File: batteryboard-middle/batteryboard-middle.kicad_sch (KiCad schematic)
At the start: 7 parts, among them J1 Conn 02x10 1.27mm, J2 Conn_01x02, J3 Conn_01x02

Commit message: modified connector arrangement
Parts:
- removed J1: Conn 02x10 1.27mm, Connector_PinHeader_1.27mm:PinHeader_2x10_P1.27mm_Vertical, symbol Connector_Generic:Conn_02x10_Odd_Even
- added J?: Conn_01x12, symbol Connector_Generic:Conn_01x12
- added J?: Conn_01x10, symbol Connector_Generic:Conn_01x10
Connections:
- new net: J?.10 (Pin_10), J?.8 (Pin_8)
- new net: J?.11 (Pin_11), J?.9 (Pin_9)
- new net: J?.10 (Pin_10), J?.12 (Pin_12)
- new net: J?.1 (Pin_1), J?.3 (Pin_3)
- new net: J?.2 (Pin_2), J?.4 (Pin_4)
- new net: J?.3 (Pin_3), J?.5 (Pin_5)
- new net: J?.4 (Pin_4), J?.6 (Pin_6)
- new net: J?.5 (Pin_5), J?.7 (Pin_7)
- new net: J?.6 (Pin_6), J?.8 (Pin_8)
- new net: J?.7 (Pin_7), J?.9 (Pin_9)
- no-connect marks 16 -> 0
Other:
- note added: "Stack Conn - From Batteryboard Bottom"
- note added: "Stack Conn - To Batteryboard Top"
- note removed: "Stack Conn"
- moved on the sheet: J2, J3

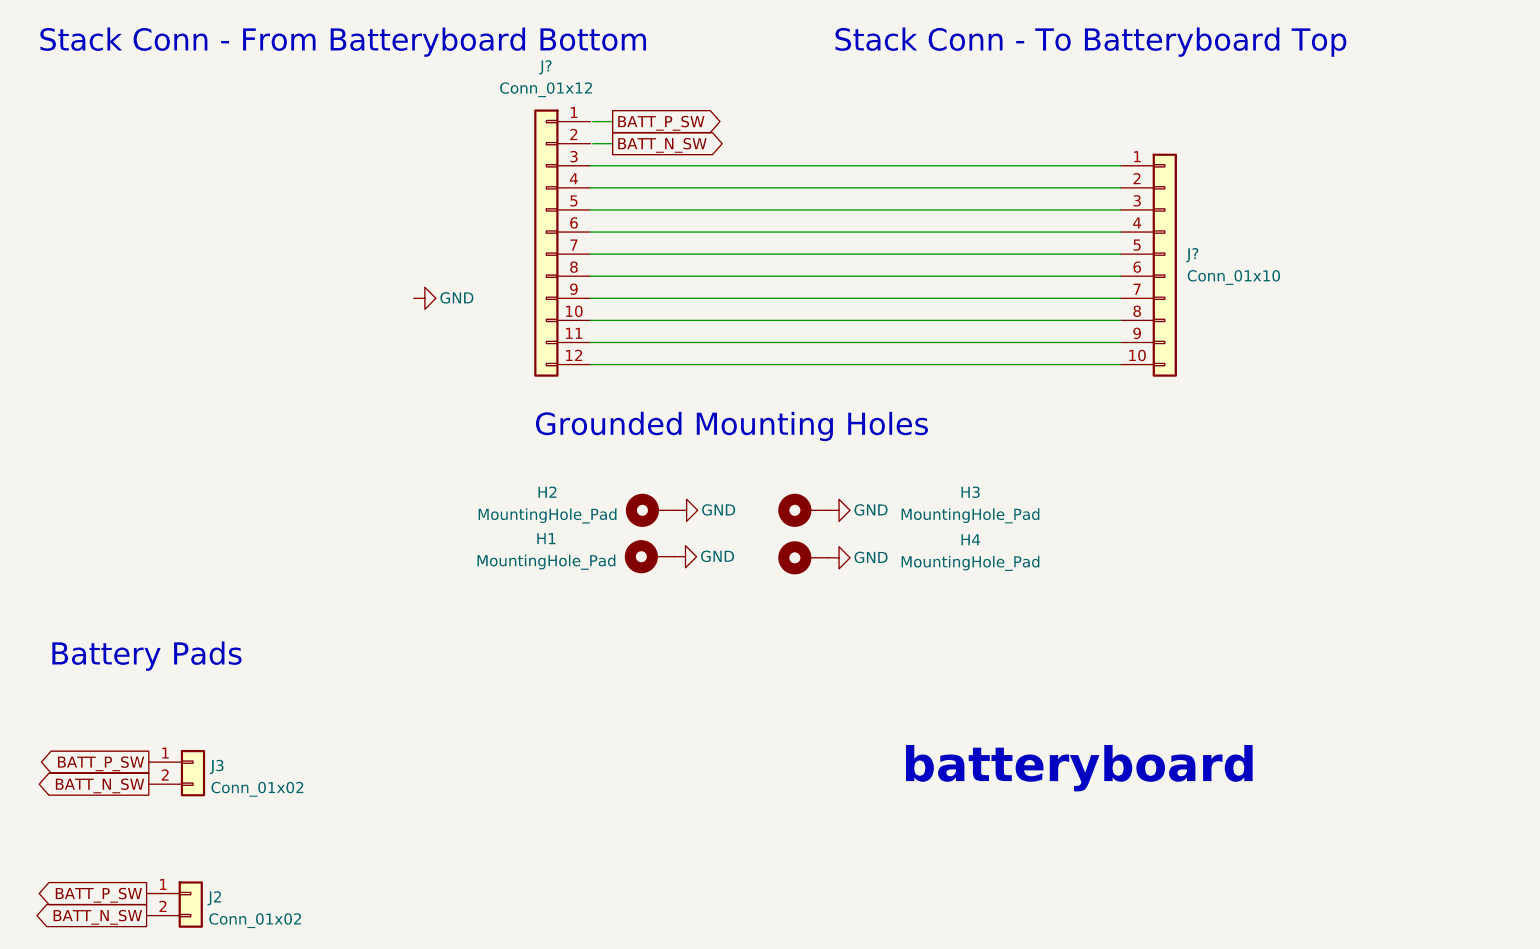
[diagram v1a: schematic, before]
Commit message: labeled connections
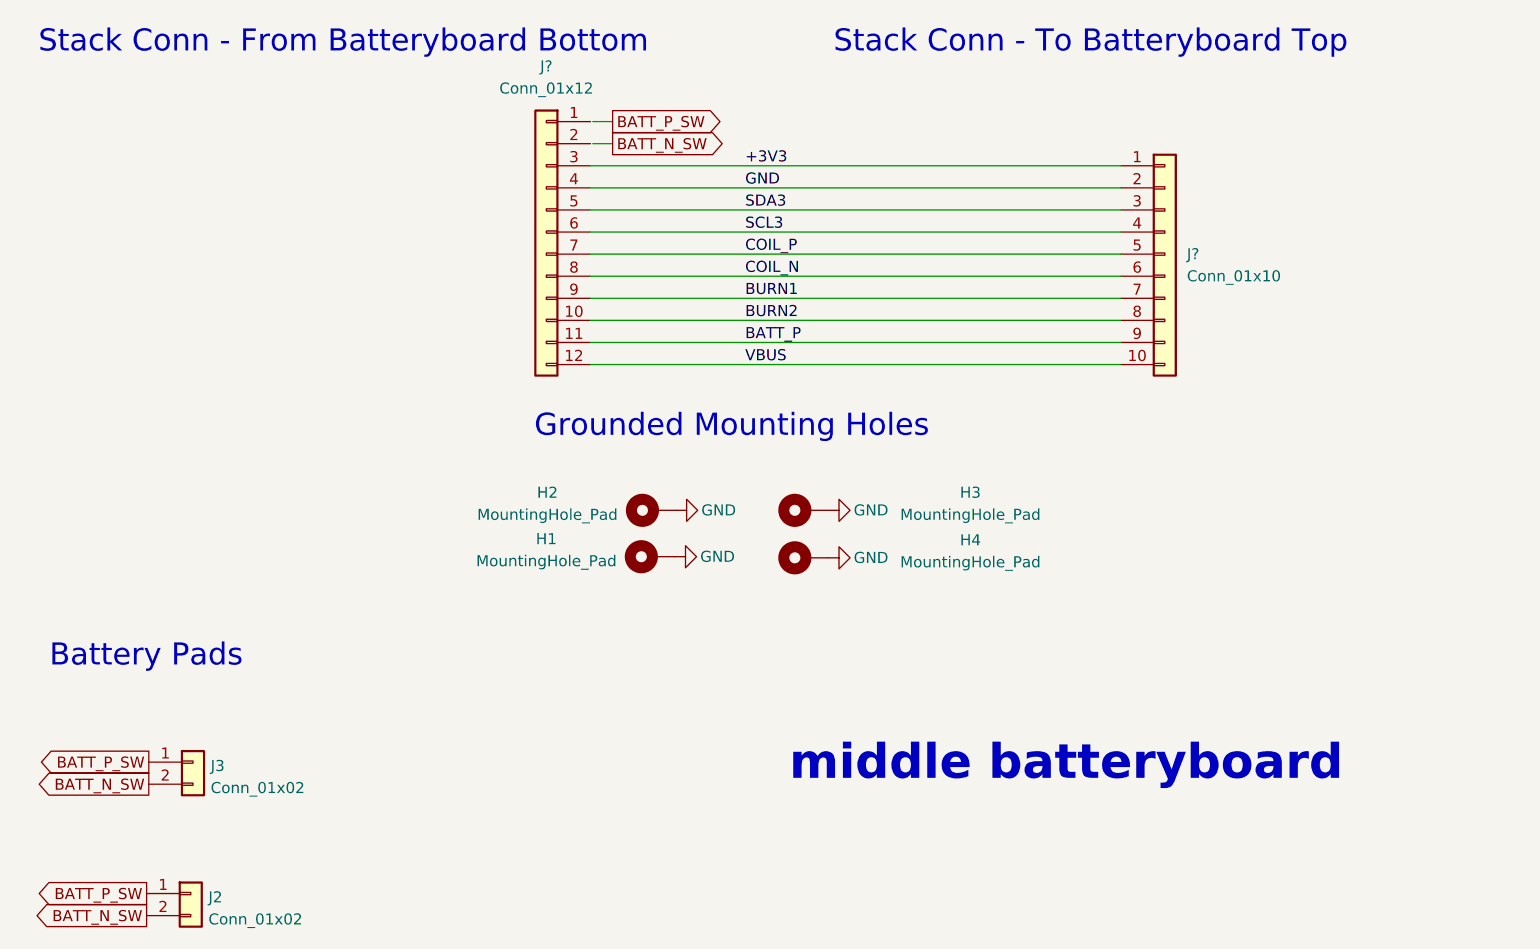
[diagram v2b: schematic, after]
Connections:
- net GND: now also J?.2 (Pin_2), J?.4 (Pin_4)
- net BURN2: now reaches J?.10 (Pin_10), J?.8 (Pin_8)
- net BATT_P: now reaches J?.11 (Pin_11), J?.9 (Pin_9)
- net VBUS: now reaches J?.10 (Pin_10), J?.12 (Pin_12)
- net +3V3: now reaches J?.1 (Pin_1), J?.3 (Pin_3)
- net SDA3: now reaches J?.3 (Pin_3), J?.5 (Pin_5)
- net SCL3: now reaches J?.4 (Pin_4), J?.6 (Pin_6)
- net COIL_P: now reaches J?.5 (Pin_5), J?.7 (Pin_7)
- net COIL_N: now reaches J?.6 (Pin_6), J?.8 (Pin_8)
- net BURN1: now reaches J?.7 (Pin_7), J?.9 (Pin_9)
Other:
- note added: "middle batteryboard"
- note removed: "batteryboard"
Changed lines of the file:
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@@
     (effects (font (size 2.54 2.54)) (justify left bottom))
   )
-  (text "batteryboard" (at 124.714 114.681 0)
+  (text "middle batteryboard" (at 111.76 114.3 0)
     (effects (font (size 3.9878 3.9878) (thickness 1.016) bold) (justify left bottom))
   )
   (text "Battery Pads" (at 26.67 101.092 0)
     (effects (font (size 2.54 2.54)) (justify left bottom))
+  )
+  (label "GND" (at 106.68 45.72 0)
+    (effects (font (size 1.27 1.27)) (justify left bottom))
+  )
+  (label "BURN1" (at 106.68 58.42 0)
+    (effects (font (size 1.27 1.27)) (justify left bottom))
+  )
+  (label "VBUS" (at 106.68 66.04 0)
+    (effects (font (size 1.27 1.27)) (justify left bottom))
+  )
+  (label "SCL3" (at 106.68 50.8 0)
+    (effects (font (size 1.27 1.27)) (justify left bottom))
+  )
+  (label "+3V3" (at 106.68 43.18 0)
+    (effects (font (size 1.27 1.27)) (justify left bottom))
+  )
+  (label "BURN2" (at 106.68 60.96 0)
+    (effects (font (size 1.27 1.27)) (justify left bottom))
+  )
+  (label "COIL_N" (at 106.68 55.88 0)
+    (effects (font (size 1.27 1.27)) (justify left bottom))
+  )
+  (label "COIL_P" (at 106.68 53.34 0)
+    (effects (font (size 1.27 1.27)) (justify left bottom))
+  )
+  (label "SDA3" (at 106.68 48.26 0)
+    (effects (font (size 1.27 1.27)) (justify left bottom))
+  )
+  (label "BATT_P" (at 106.68 63.5 0)
+    (effects (font (size 1.27 1.27)) (justify left bottom))
   )
   (global_label "BATT_P_SW" (shape output) (at 37.846 126.873 180) (fields_autoplaced)
@@
       (effects (font (size 1.27 1.27)) (justify right) hide)
     )
-  )
-  (symbol (lib_id "power:GND") (at 68.58 58.42 90) (unit 1)
-    (in_bom yes) (on_board yes)
-    (property "Reference" "#PWR?" (id 0) (at 74.93 58.42 0)
-      (effects (font (size 1.27 1.27)) hide)
-    )
-    (property "Value" "GND" (id 1) (at 73.533 58.42 90))
-    (property "Footprint" "" (id 2) (at 68.58 58.42 0)
-      (effects (font (size 1.27 1.27)) hide)
-    )
-    (property "Datasheet" "" (id 3) (at 68.58 58.42 0)
-      (effects (font (size 1.27 1.27)) hide)
-    )
-    (pin "1")
   )
   (symbol (lib_id "Connector_Generic:Conn_01x12") (at 83.82 50.8 0) (mirror y) (unit 1)
@@
       (reference "#PWR0106") (unit 1) (value "GND") (footprint "")
     )
-    (path "/1bdfede1-22a7-4a7e-8979-e030eca04f8f"
-      (reference "#PWR?") (unit 1) (value "GND") (footprint "")
-    )
     (path "/5a4e0212-db20-4e54-af24-453bc0252d21"

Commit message: switch to 2x connectors for battery boards
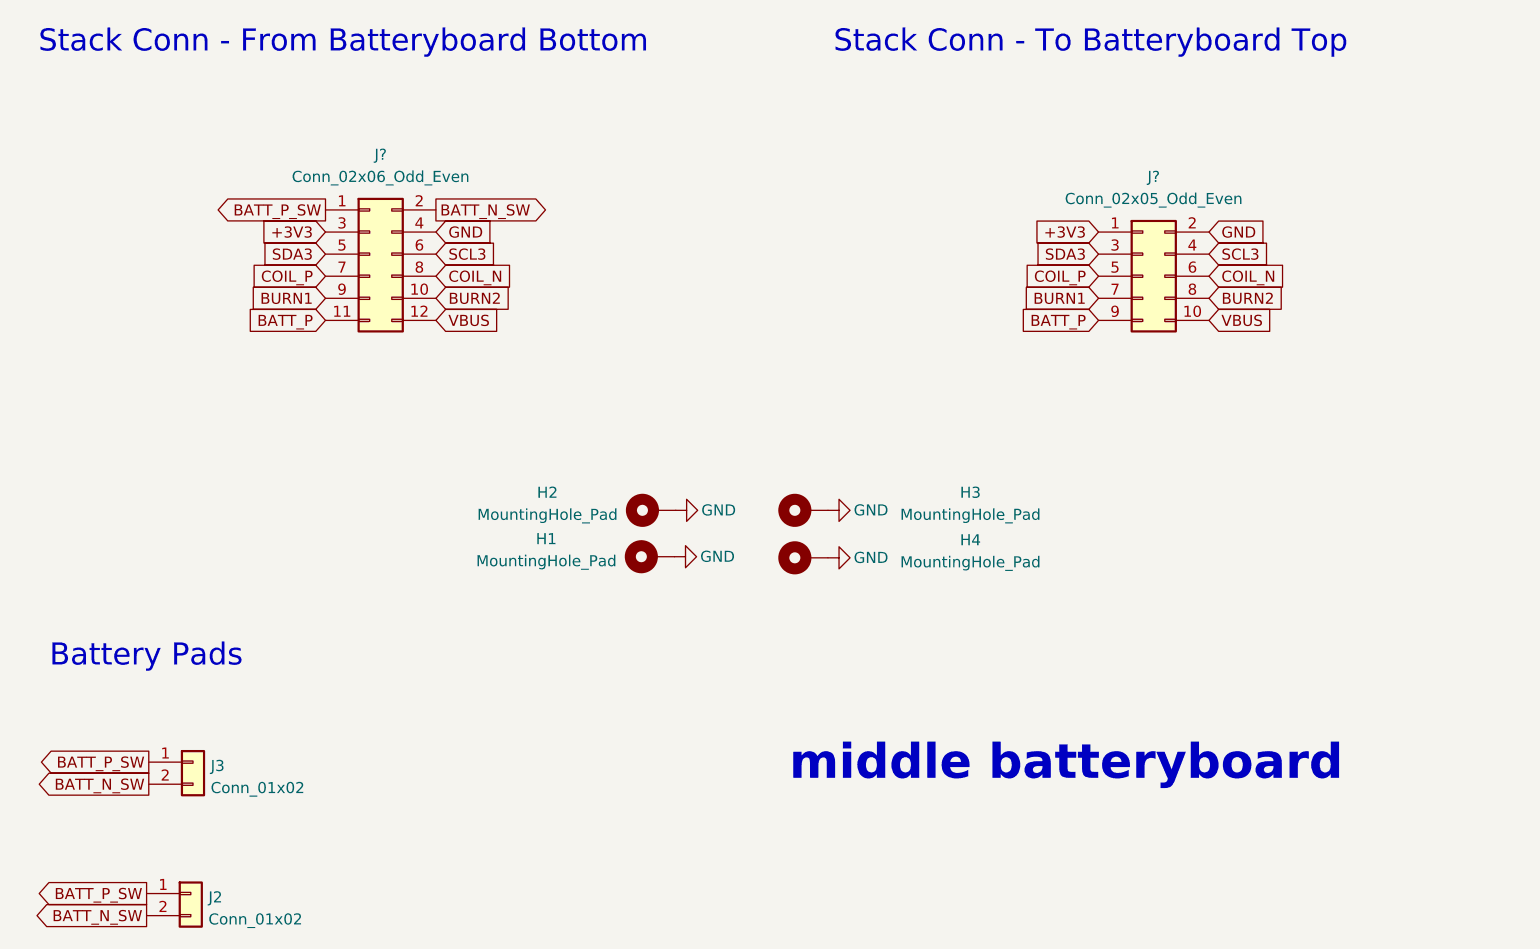
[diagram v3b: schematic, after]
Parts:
- removed J?: Conn_01x12, symbol Connector_Generic:Conn_01x12
- removed J?: Conn_01x10, symbol Connector_Generic:Conn_01x10
- added J?: Conn_02x06_Odd_Even, symbol Connector_Generic:Conn_02x06_Odd_Even
- added J?: Conn_02x05_Odd_Even, symbol Connector_Generic:Conn_02x05_Odd_Even
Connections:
- net +3V3: now also J?.1 (Pin_1), J?.3 (Pin_3)
- net BATT_N_SW: now also J?.2 (Pin_2)
- net BATT_P: now also J?.11 (Pin_11), J?.9 (Pin_9)
- net BATT_P_SW: now also J?.1 (Pin_1)
- net BURN1: now also J?.7 (Pin_7), J?.9 (Pin_9)
- net BURN2: now also J?.10 (Pin_10), J?.8 (Pin_8)
- net COIL_N: now also J?.6 (Pin_6), J?.8 (Pin_8)
- net COIL_P: now also J?.5 (Pin_5), J?.7 (Pin_7)
- net GND: now also J?.2 (Pin_2), J?.4 (Pin_4)
- net SCL3: now also J?.4 (Pin_4), J?.6 (Pin_6)
- net SDA3: now also J?.3 (Pin_3), J?.5 (Pin_5)
- net VBUS: now also J?.10 (Pin_10), J?.12 (Pin_12)
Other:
- note removed: "Grounded Mounting Holes"

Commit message: remove burn wire signals
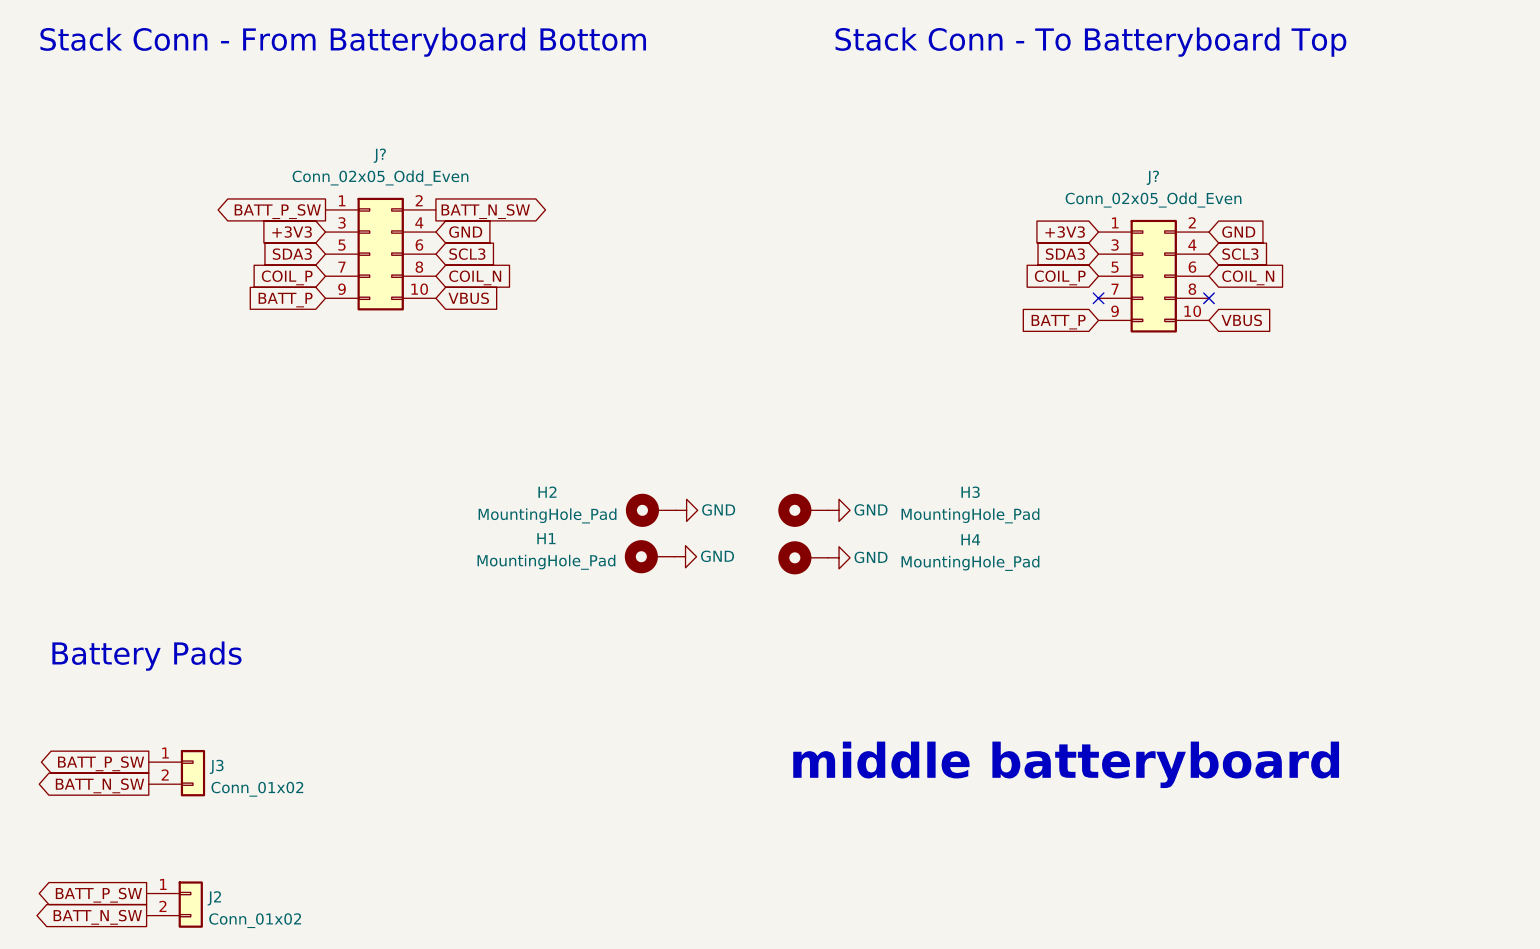
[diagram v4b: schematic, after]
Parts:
- removed J?: Conn_02x06_Odd_Even, symbol Connector_Generic:Conn_02x06_Odd_Even
- added J?: Conn_02x05_Odd_Even, symbol Connector_Generic:Conn_02x05_Odd_Even
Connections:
- net +3V3: now also J?.3 (Pin_3)
- net BATT_N_SW: now also J?.2 (Pin_2)
- net BATT_P: now also J?.9 (Pin_9)
- net BATT_P_SW: now also J?.1 (Pin_1)
- net COIL_N: now also J?.8 (Pin_8)
- net COIL_P: now also J?.7 (Pin_7)
- net GND: now also J?.4 (Pin_4)
- net SCL3: now also J?.6 (Pin_6)
- net SDA3: now also J?.5 (Pin_5)
- net VBUS: now also J?.10 (Pin_10)
- net BURN1: no longer names the net of J?.7 (Pin_7)
- net BURN2: no longer names the net of J?.8 (Pin_8)
- no-connect marks 0 -> 2

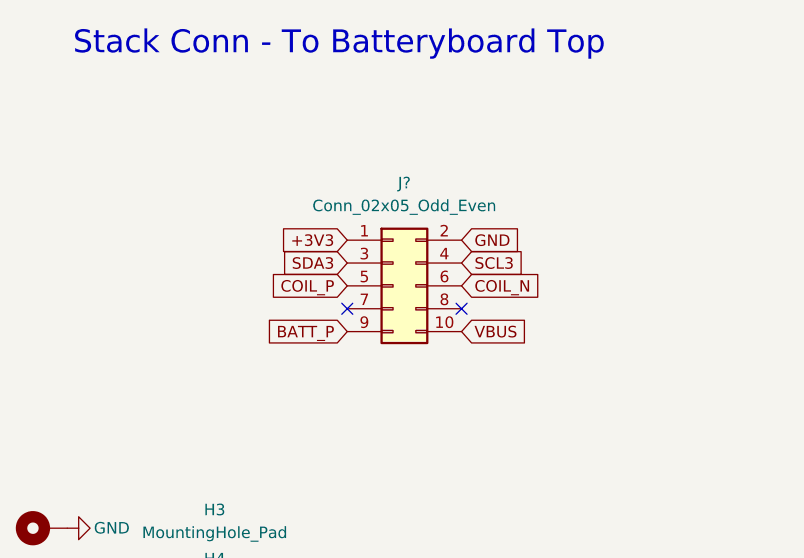
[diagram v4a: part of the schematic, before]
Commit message: NC on pins 1 and 2 to match with -Y
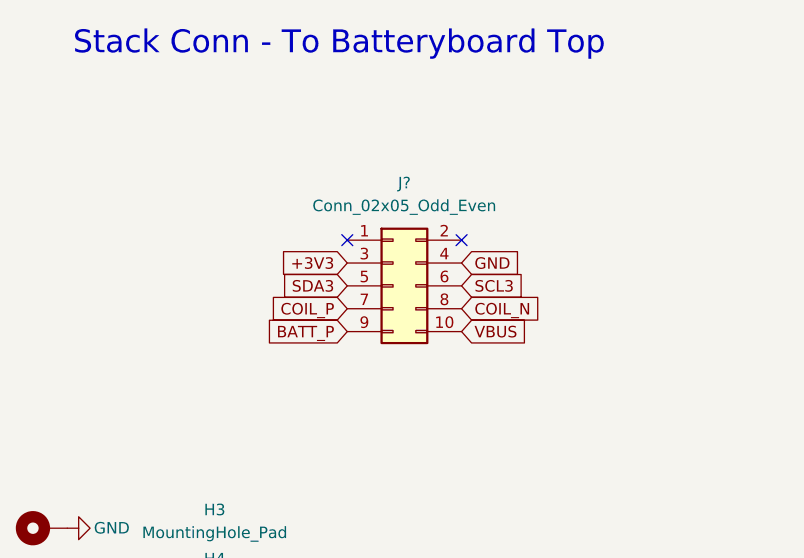
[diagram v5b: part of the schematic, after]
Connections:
- net +3V3: now also J?.3 (Pin_3); no longer J?.1 (Pin_1)
- net COIL_N: now also J?.8 (Pin_8); no longer J?.6 (Pin_6)
- net COIL_P: now also J?.7 (Pin_7); no longer J?.5 (Pin_5)
- net GND: now also J?.4 (Pin_4); no longer J?.2 (Pin_2)
- net SCL3: now also J?.6 (Pin_6); no longer J?.4 (Pin_4)
- net SDA3: now also J?.5 (Pin_5); no longer J?.3 (Pin_3)
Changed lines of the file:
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@@
     (comment 1 "N. Khera")
   )
-  (no_connect (at 147.32 58.42))
-  (no_connect (at 160.02 58.42))
+  (no_connect (at 160.02 50.8))
+  (no_connect (at 147.32 50.8))
   (text "Stack Conn - To Batteryboard Top" (at 116.84 30.48 0)
     (effects (font (size 2.54 2.54)) (justify left bottom))
@@
     )
   )
-  (global_label "SDA3" (shape input) (at 147.32 53.34 180) (fields_autoplaced)
+  (global_label "SDA3" (shape input) (at 147.32 55.88 180) (fields_autoplaced)
     (effects (font (size 1.27 1.27)) (justify right))
-    (property "Intersheet References" "${INTERSHEET_REFS}" (id 0) (at 140.1293 53.2606 0)
+    (property "Intersheet References" "${INTERSHEET_REFS}" (id 0) (at 140.1293 55.8006 0)
       (effects (font (size 1.27 1.27)) (justify right) hide)
     )
@@
     )
   )
-  (global_label "+3V3" (shape input) (at 147.32 50.8 180) (fields_autoplaced)
+  (global_label "+3V3" (shape input) (at 147.32 53.34 180) (fields_autoplaced)
     (effects (font (size 1.27 1.27)) (justify right))
-    (property "Intersheet References" "${INTERSHEET_REFS}" (id 0) (at 139.8269 50.7206 0)
+    (property "Intersheet References" "${INTERSHEET_REFS}" (id 0) (at 139.8269 53.2606 0)
       (effects (font (size 1.27 1.27)) (justify right) hide)
     )
@@
     )
   )
-  (global_label "COIL_N" (shape input) (at 160.02 55.88 0) (fields_autoplaced)
+  (global_label "COIL_N" (shape input) (at 160.02 58.42 0) (fields_autoplaced)
     (effects (font (size 1.27 1.27)) (justify left))
-    (property "Intersheet References" "${INTERSHEET_REFS}" (id 0) (at 168.9645 55.8006 0)
+    (property "Intersheet References" "${INTERSHEET_REFS}" (id 0) (at 168.9645 58.3406 0)
       (effects (font (size 1.27 1.27)) (justify left) hide)
     )
@@
     )
   )
-  (global_label "COIL_P" (shape input) (at 147.32 55.88 180) (fields_autoplaced)
+  (global_label "COIL_P" (shape input) (at 147.32 58.42 180) (fields_autoplaced)
     (effects (font (size 1.27 1.27)) (justify right))
-    (property "Intersheet References" "${INTERSHEET_REFS}" (id 0) (at 138.4359 55.8006 0)
+    (property "Intersheet References" "${INTERSHEET_REFS}" (id 0) (at 138.4359 58.3406 0)
       (effects (font (size 1.27 1.27)) (justify right) hide)
     )
   )
-  (global_label "GND" (shape input) (at 160.02 50.8 0) (fields_autoplaced)
+  (global_label "GND" (shape input) (at 160.02 53.34 0) (fields_autoplaced)
     (effects (font (size 1.27 1.27)) (justify left))
-    (property "Intersheet References" "${INTERSHEET_REFS}" (id 0) (at 166.3036 50.7206 0)
+    (property "Intersheet References" "${INTERSHEET_REFS}" (id 0) (at 166.3036 53.2606 0)
       (effects (font (size 1.27 1.27)) (justify left) hide)
     )
@@
     )
   )
-  (global_label "SCL3" (shape input) (at 160.02 53.34 0) (fields_autoplaced)
+  (global_label "SCL3" (shape input) (at 160.02 55.88 0) (fields_autoplaced)
     (effects (font (size 1.27 1.27)) (justify left))
-    (property "Intersheet References" "${INTERSHEET_REFS}" (id 0) (at 167.1502 53.2606 0)
+    (property "Intersheet References" "${INTERSHEET_REFS}" (id 0) (at 167.1502 55.8006 0)
       (effects (font (size 1.27 1.27)) (justify left) hide)
     )
